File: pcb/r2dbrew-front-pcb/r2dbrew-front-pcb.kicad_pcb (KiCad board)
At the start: 2 copper layers, 44.4 x 61 mm, 137 parts, among them IC1 ATTINY167, IC2 LM1117, J1 6-12V, M3 VAL**, P1 AVR_ISP, Q1 DDTB113ZC, Q10 DDTB113ZC, Q11 DDTD113ZC, Q12 DDTD113ZC, Q13 DDTB113ZC, Q14 DDTD113ZC, Q15 DDTD113ZC, Q2 DDTB113ZC, Q3 DDTD113ZC, Q4 DDTD113ZC, Q5 DDTB113ZC, Q6 DDTB113ZC, Q7 DDTD113ZC, Q8 DDTD113ZC, Q9 DDTB113ZC

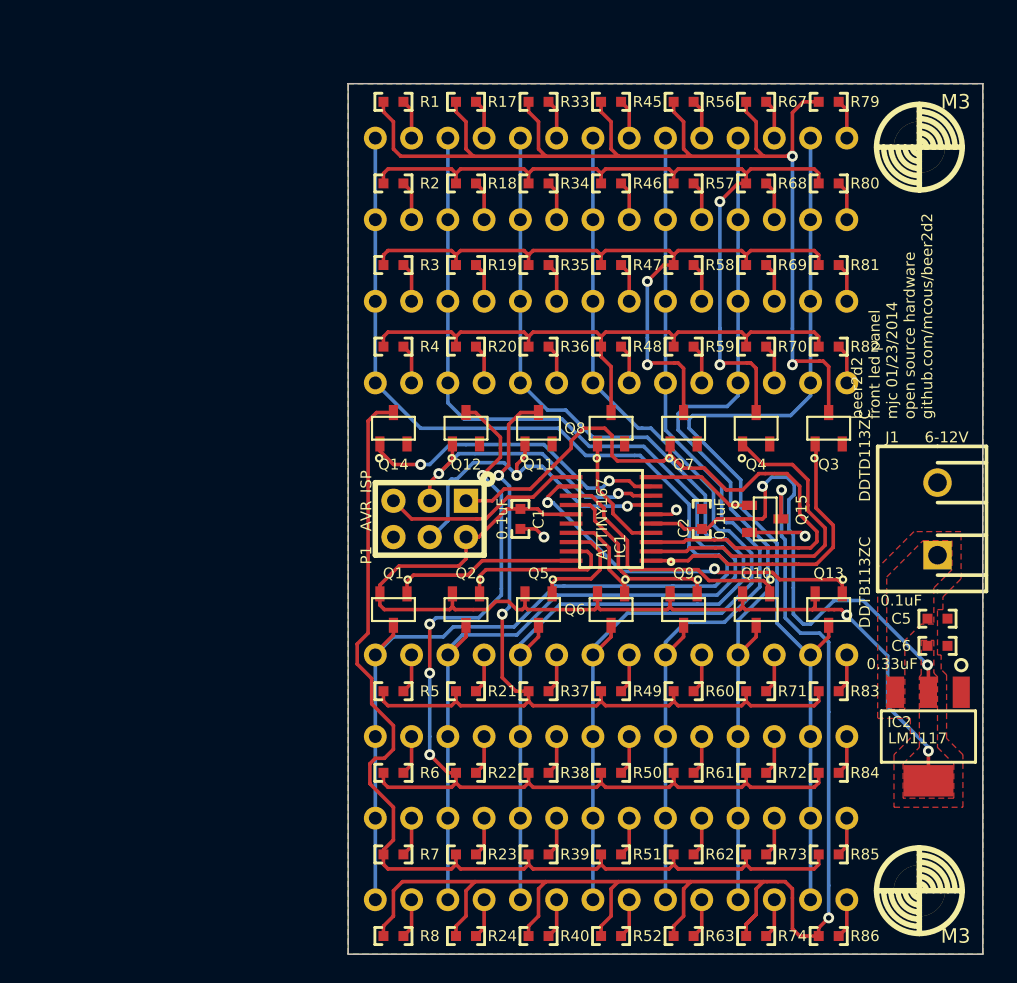
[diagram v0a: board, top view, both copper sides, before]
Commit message: cleanup files after rename and prepare for plotting
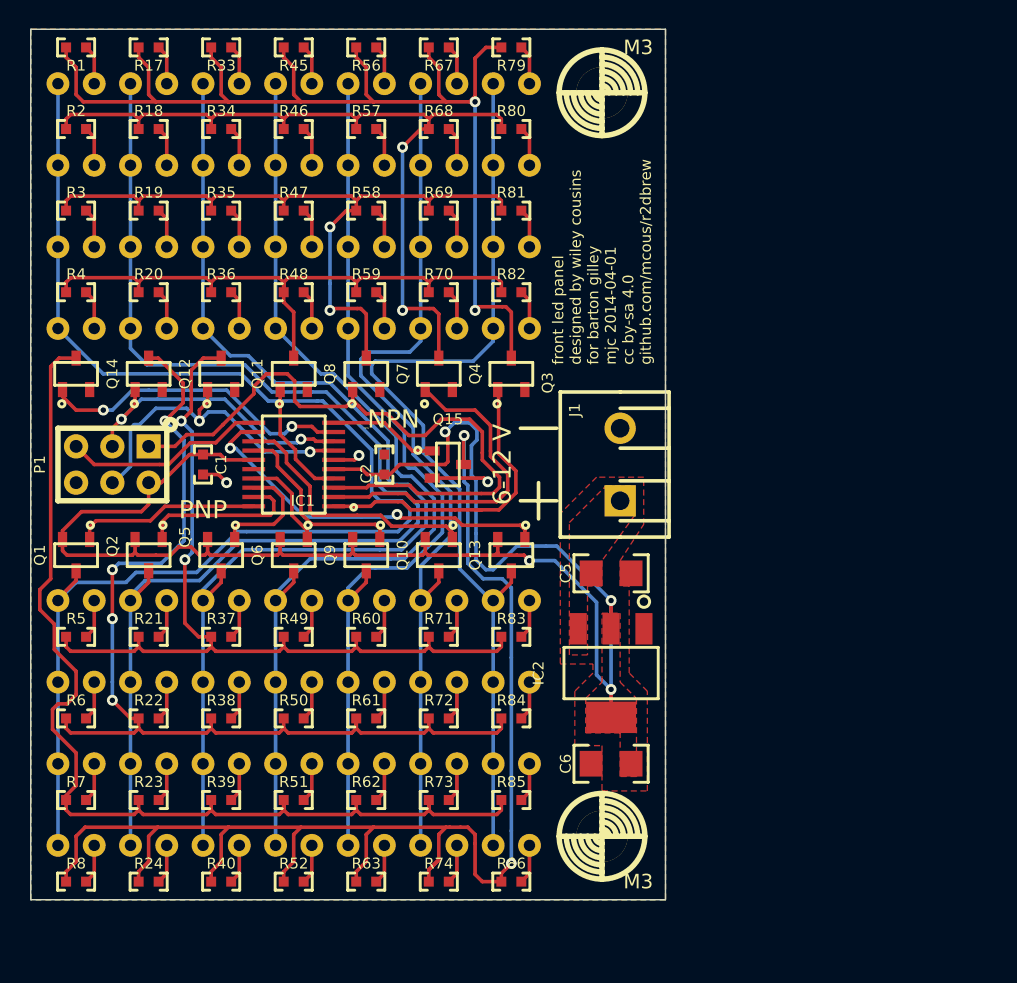
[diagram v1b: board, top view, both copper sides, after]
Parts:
- C1, C2, R1, R17, R18, R19, R2, R20, R21, R22, R23, R24, R3, R33, R34, R35, R36, R37, R38, R39, R4, R40, R45, R46, R47, R48, R49, R5, R50, R51, R52, R56, R57, R58, R59, R6, R60, R61, R62, R63, R67, R68, R69, R7, R70, R71, R72, R73, R74, R79, R8, R80, R81, R82, R83, R84, R85, R86: footprint 0603(1608m) -> passive-smd:0603(1608m)
- C5: value 0.1uF -> 10uF; footprint 0603(1608m) -> passive-smd:1206(3216m)
- C6: value 0.33uF -> 22uF; footprint 0603(1608m) -> passive-smd:1206(3216m)
- IC1: footprint TSSOP20 -> sop:TSSOP20
- IC2: footprint SOT223 -> sot:SOT223
- J1: footprint 2-PIN_SCREW-TERM_P200MIL -> connect-thru:1x2-SCREW-TERM_P200mil
- LED1, LED10, LED11, LED12, LED13, LED14, LED15, LED16, LED17, LED18, LED19, LED2, LED20, LED21, LED22, LED23, LED24, LED25, LED26, LED27, LED28, LED29, LED3, LED30, LED31, LED32, LED33, LED34, LED35, LED36, LED37, LED38, LED39, LED4, LED40, LED41, LED42, LED43, LED44, LED45, LED46, LED47, LED48, LED49, LED5, LED50, LED51, LED52, LED53, LED54, LED55, LED56, LED6, LED7, LED8, LED9: footprint LED-5mm -> led:5mm-THRU-LED
- P1: footprint 2x3-array -> connect-thru:2x3-ARRAY_P100mil
- Q1, Q10, Q11, Q12, Q13, Q14, Q15, Q2, Q3, Q4, Q5, Q6, Q7, Q8, Q9: footprint SOT23 -> sot:SOT23
- moved C6 24.3 mm to (152.4, 125.1), turned to 180 degrees
- moved C5 23.1 mm to (152.4, 111.8)
- moved IC2 22.7 mm to (152.4, 118.7)
- moved M3 22.5 mm to (151.8, 130.2)
- moved M3 22.5 mm to (151.8, 78.1)
- moved C1 22.5 mm to (123.8, 104.1)
- moved LED10 22.5 mm to (120.0, 83.2), turned to 180 degrees
- moved LED11 22.5 mm to (120.0, 88.9), turned to 180 degrees
- moved LED12 22.5 mm to (120.0, 94.6), turned to 180 degrees
- moved LED13 22.5 mm to (120.0, 113.7), turned to 180 degrees
- moved LED14 22.5 mm to (120.0, 119.4), turned to 180 degrees
- moved LED15 22.5 mm to (120.0, 125.1), turned to 180 degrees
- moved LED16 22.5 mm to (120.0, 130.8), turned to 180 degrees
- moved LED9 22.5 mm to (120.0, 77.5), turned to 180 degrees
- moved Q12 22.5 mm to (120.0, 97.8)
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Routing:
- net VCC: track 108.9 -> 115.4 mm
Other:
- board size 44.4 x 61 mm -> 44.5 x 61 mm
- board text added: "6-12 V"
- board text added: "NPN"
- board text added: "PNP"
- board text added: "front led panel designed by wiley cousins for barton gilley mjc 2014-04-01 cc by-sa 4.0 github.com/mcous/r2dbrew"
- board text removed: "beer2d2 front led panel mjc 01/23/2014 open source hardware github.com/mcous/beer2d2"

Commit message: fix rear silkscreen and mask clearance
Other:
- rule pad_to_mask_clearance: 0 -> 0.0762
